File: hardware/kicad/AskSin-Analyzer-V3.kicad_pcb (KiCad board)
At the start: 4 copper layers, 88 x 42 mm, 38 parts, among them J1 Pi GPIO, J2 AVR-ISP-6, J5 OLED I2C, J6 Taster, J7 WS2812, U1 MCP1754S-3302xCB, U2 ATmega328P-AU, U3 E07-900M10S, Y1 8MHz

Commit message: R5 von 0 Ohm auf 330 Ohm — der Serienwiderstand des Vorbilds fehlte
Das Status-LED-OLED-Projekt fuehrt die WS2812-Datenleitung fuer *beide*
Ansteuerarten ueber 330-470 Ohm. Auf dem SPI-Weg war R5 bei uns eine
0-Ohm-Bruecke, der Widerstand fehlte dort also ganz. Jetzt 330 Ohm —
dasselbe Bauteil wie R1 (JLCPCB C17630), damit faellt sogar eine
Position in der Stueckliste weg (10 statt 11).

Signaltechnisch geprueft: 330 Ohm an der Eingangskapazitaet der LED
ergibt rund 5 ns Anstiegszeit gegen 420 ns kuerzeste Pulsdauer bei
2,4 MHz — unkritisch.

DRC 0/0, Netzliste exakt, alle Massepads angebunden.

Co-Authored-By: Claude Opus 5 <noreply@anthropic.com>
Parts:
- R5: value 0R -> 330
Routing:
- net GND: track 31.8 -> 56.5 mm, vias 131 -> 147
- net +3V3: track 134.5 -> 152.2 mm
- net MISO: track 71.8 -> 82.2 mm
- net PI_RESET_DRV: track 46.2 -> 39.8 mm
- net WS_DATA: track 8.16 -> 11.7 mm
- net UART_PI_TX: track 50.3 -> 52.7 mm, vias 2 -> 1
- net RESET: track 56.9 -> 54.9 mm, vias 1 -> 2
- net LED_PWM: track 33.4 -> 35.2 mm
- net SCK: track 66.3 -> 64.7 mm
- net MOSI: track 57.8 -> 56.3 mm, vias 3 -> 2
- net PI_3V3: track 77.9 -> 76.4 mm
- net XTAL1: track 9.97 -> 8.57 mm
- net LED_TREIBER: track 21.6 -> 22.6 mm
- net LED_SPI: track 28.4 -> 29.1 mm
- net CS: track 86.8 -> 87.5 mm

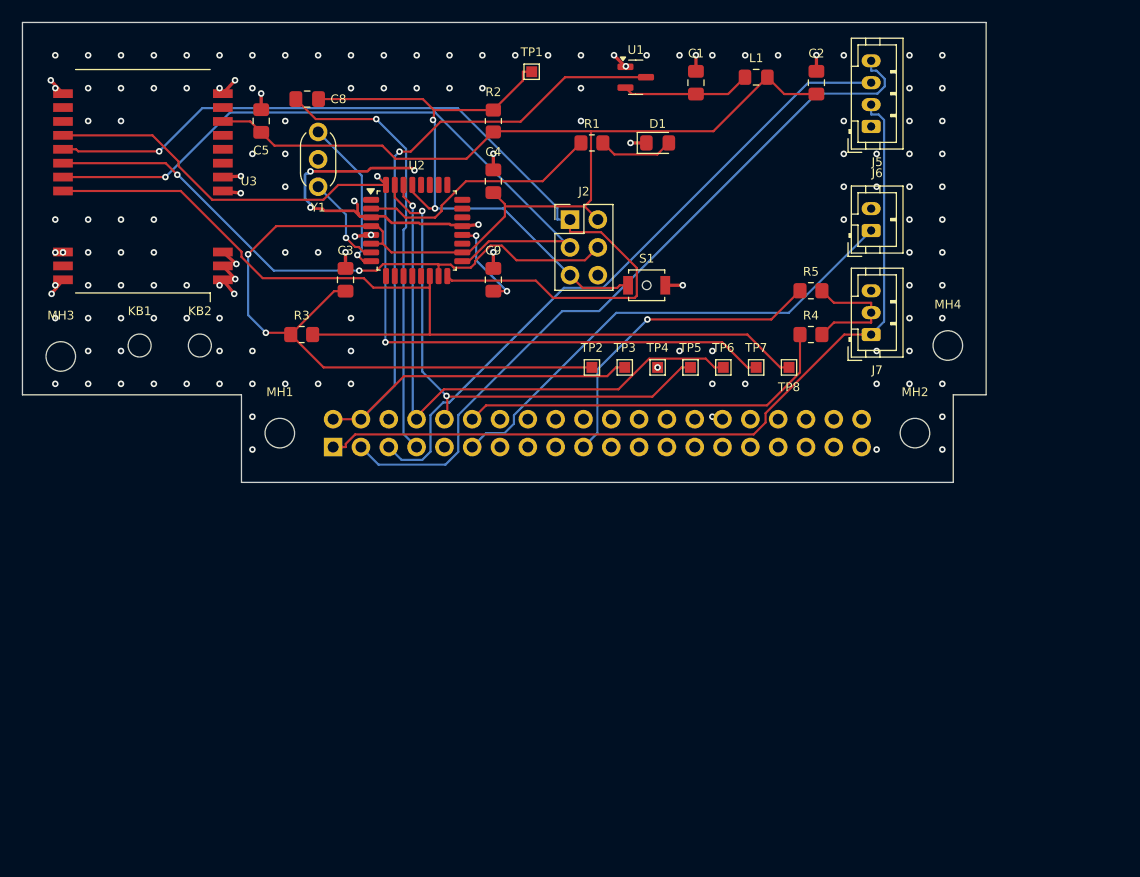
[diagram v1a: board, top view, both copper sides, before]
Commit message: Platine v0.2.0: L-Form neben dem Pi, Umschalter statt Bestueckungsvariante
Neue Bauform nach Silvios Vorgaben: Streifen hoechstens 20 mm neben dem
Pi (vorher 34), bis 80 mm lang, Schenkel an der SD-Kante entlang. Ueber
dem Pi liegt nur der 8 mm tiefe Arm fuer die 2x20-Buchse und eine
7 x 9 mm grosse Nase am hinteren Befestigungsloch — der Luefter des
PoE-HAT bleibt frei, unabhaengig vom Modell. Vier Schraubpunkte: zwei
HAT-Bohrungen im Arm, das hintere Pi-Loch in der Nase, eines im
Schenkel fuer den Tray.

Pi-Masse aus den amtlichen Zeichnungen geprueft: 85 x 56 mm, Loecher
58 x 49 mm, 3,5 mm von den Kanten — bei Pi 3B+, 4 und 5 identisch. Beim
PoE HAT (F) beginnt der Luefter rund 20 mm hinter der SD-Kante.

R4/R5 als Bestueckungsvariante entfallen. Stattdessen SPDT-Schiebe-
schalter SW1 (C&K JS102011SAQN, JLCPCB C221660) an der Aussenkante plus
EIN gemeinsamer 330-Ohm-Widerstand. Bewusst dieser Typ und nicht der
billigere MSK-12C02: fuer den JS102011SAQN gibt es einen amtlichen
KiCad-Footprint, der MSK haette von Hand gezeichnet werden muessen —
seine Landzeichnung hat ungleich verteilte Pads, das ist genau die
Sorte Fehlerquelle, die wir uns nicht leisten koennen.

Zwei eigene Fehler unterwegs gefunden und behoben: Der Innenversatz der
Kontur lief an den einspringenden Ecken in die falsche Richtung, wodurch
Freerouting Bahnen ueber die Platinenkante legte; und der Versuch, In2
als dritte Signallage freizugeben, erzeugte 120 Verstoesse inklusive
echter Kurzschluesse, weil die Stuetzvias durchgehend sind — beides
zurueckgenommen bzw. korrigiert und im Code kommentiert.

ERC 0/0, DRC 0/0, Netzliste exakt gegen die Spezifikation, alle
Massepads angebunden, J1-Pads gegen das Pi-Raster geprueft.
Fertigungspaket neu erzeugt (11 Positionen, davon 7 Basic).

Co-Authored-By: Claude Opus 5 <noreply@anthropic.com>
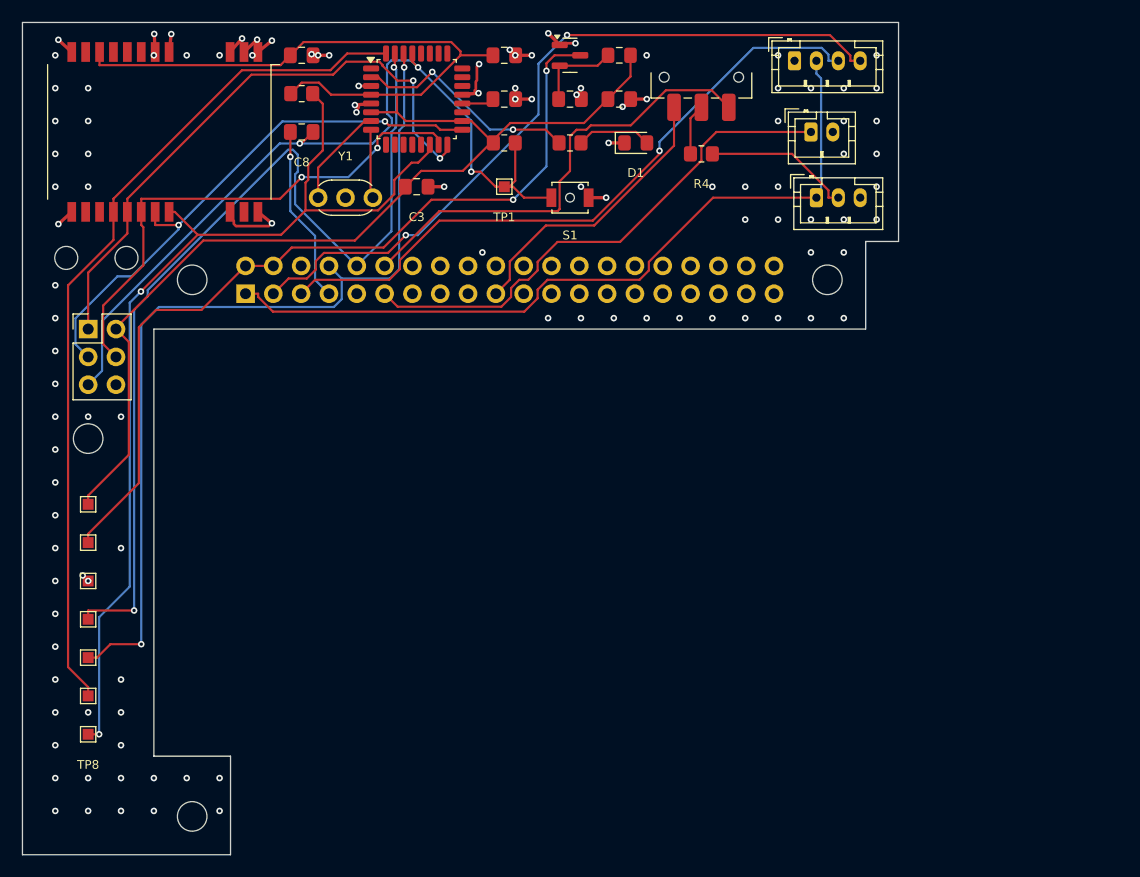
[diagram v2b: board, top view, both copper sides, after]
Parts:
- removed R5: 330, R_0805_2012Metric_Pad1.20x1.40mm_HandSolder
- added SW1: PWM/SPI, SW_SPDT_CK_JS102011SAQN, F.Cu at (162.0, 65.0)
- R4: value 390 DNP -> 330
- moved MH4 79.0 mm to (106.0, 98.0)
- moved TP8 72.2 mm to (106.0, 125.0)
- moved TP7 68.0 mm to (106.0, 121.5)
- moved TP6 63.8 mm to (106.0, 118.0)
- moved TP5 59.6 mm to (106.0, 114.5)
- moved TP4 55.5 mm to (106.0, 111.0)
- moved TP3 51.5 mm to (106.0, 107.5)
- moved TP2 47.7 mm to (106.0, 104.0)
- moved J2 45.1 mm to (106.0, 88.0)
- moved MH3 43.7 mm to (115.5, 132.5)
- moved R3 22.0 mm to (125.5, 66.5)
- moved R4 19.3 mm to (162.0, 72.0)
- moved C2 18.1 mm to (154.5, 67.0), turned to 0 degrees
- moved C9 16.5 mm to (144.0, 67.0), turned to 0 degrees
- moved J1 16.1 mm to (120.4, 84.8)
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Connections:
- R4 pad 1: LED_PWM -> WS_WAHL
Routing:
- net UART_328_TX: track 47.7 -> 87.6 mm
- net UART_PI_TX: track 52.7 -> 82.8 mm, vias 1 -> 2
- net MISO: track 82.2 -> 55.1 mm, vias 1 -> 2
- net PI_RESET_DRV: track 39.8 -> 16.2 mm
- net RESET: track 54.9 -> 76.3 mm, vias 2 -> 3
- net GND: track 56.5 -> 37.8 mm, vias 147 -> 114
- net SCK: track 64.7 -> 50.7 mm, vias 1 -> 2
- net MOSI: track 56.3 -> 47.4 mm
- net XTAL2: track 14.6 -> 6.31 mm, vias 1 -> 0
- net LED_PWM: track 35.2 -> 42.1 mm
- net GDO0: track 84.1 -> 78.3 mm, vias 2 -> 0
- net AREF: track 8.77 -> 2.97 mm, vias 2 -> 0
- net PI_3V3: track 76.4 -> 71.1 mm
- net +3V3: track 152.2 -> 147.4 mm, vias 2 -> 0
- net WS_WAHL: track 0.00 -> 4.66 mm
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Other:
- board size 88 x 42 mm -> 80 x 76 mm

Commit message: Platine 100 mm lang, Schalter beschriftet, Fertigungspruefung als Skript
Laenge von 80 auf 100 mm — die zusaetzliche Flaeche entspannt Routing und
Bestueckungsdruck deutlich; der Streifen neben dem Pi bleibt bei 20 mm.
Fuenfter Schraubpunkt am vorderen Ende fuer den Tray.

Der Umschalter traegt jetzt „PWM" und „SPI" im Bestueckungsdruck. Die
Beschriftung benennt bewusst die **Anschluesse** (Pin 1 = GPIO18,
Pin 3 = GPIO10), nicht die Schieberstellungen: welche Stellung welchen
Anschluss durchschaltet, gibt C&K nicht frei zugaenglich her, die
Pinbelegung dagegen steht fest. Positionen leiten sich aus den echten
Pads ab, folgen also einer Umplatzierung automatisch.

Neu: pruefe_fertigung.py — 17 maschinelle Pruefungen ueber das hinaus,
was DRC und Netzlistenvergleich abdecken: Lagenaufbau, geschlossener
Umriss, kleinster Bohrer und Via-Ring gegen die Herstellermindestmasse,
Bohrbild gegen das Pi-Raster, J1 gegen die HAT-Vorlage, Polung der
Status-LED, Verdrahtung und Beschriftung des Schalters, Vollstaendigkeit
des Archivs, Deckungsgleichheit von BOM/CPL/Platine.

Das Skript hat prompt zwei Abweichungen gemeldet — beide in ihm selbst:
Der Ursprung kam aus der Bounding-Box, die die halbe Linienbreite der
Umrisskante mitzaehlt (0,05 mm Versatz gegen die Fertigungsdaten). Jetzt
rechnet es aus den Kantensegmenten. Ausserdem meidet die Beschriftungs-
routine nun jedes einzelne Pad, nicht nur Bauteilumrisse.

Ergebnis: DRC 0/0, ERC 0/0, Netzliste exakt, alle 17 Pruefungen bestanden.

Co-Authored-By: Claude Opus 5 <noreply@anthropic.com>
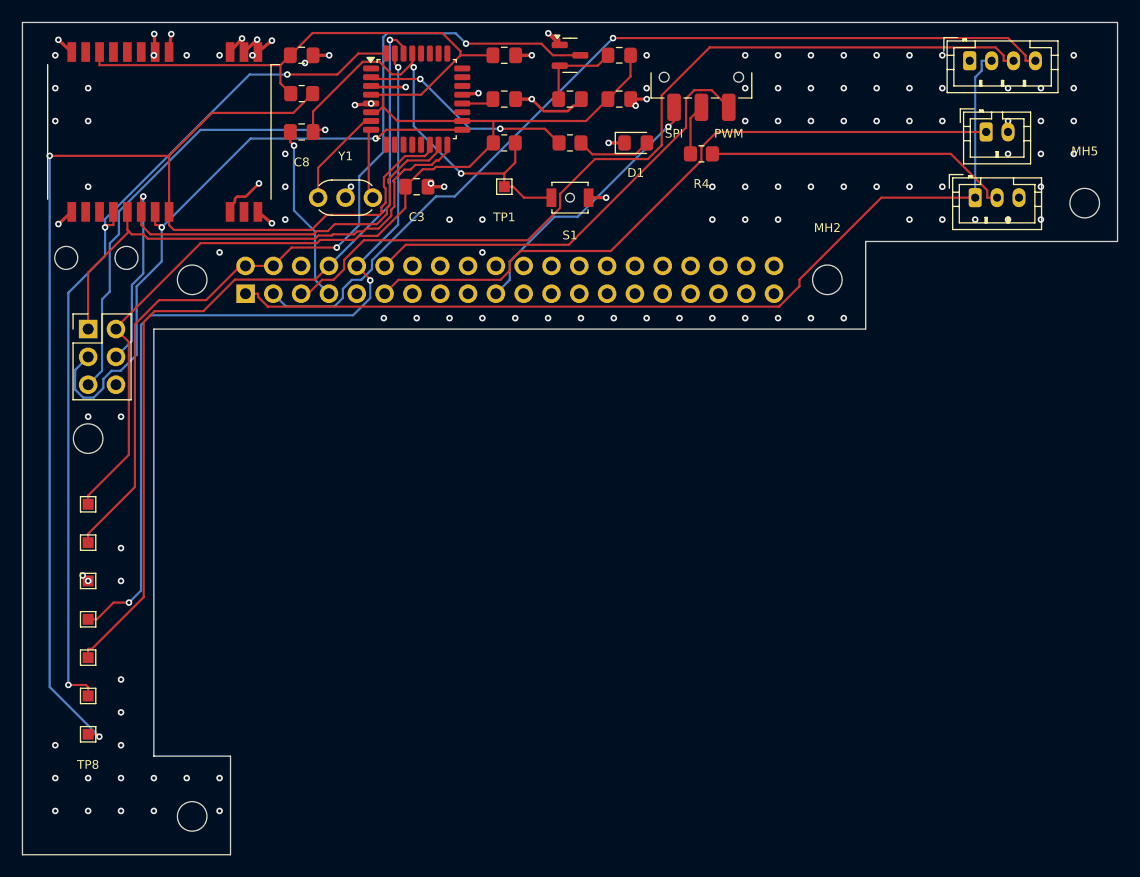
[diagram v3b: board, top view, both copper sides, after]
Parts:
- added MH5: MountingHole_2.7mm_M2.5, MountingHole_2.7mm_M2.5, F.Cu at (197.0, 76.5)
- moved J5 16.0 mm to (186.5, 63.5)
- moved J6 16.0 mm to (188.0, 70.0)
- moved J7 14.5 mm to (187.0, 76.0)
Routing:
- net CS: track 91.2 -> 118.2 mm
- net I2C_SCL: track 60.3 -> 79.1 mm, vias 1 -> 0
- net BTN: track 47.7 -> 62.2 mm
- net I2C_SDA: track 67.8 -> 82.3 mm, vias 2 -> 1
- net WS_DATA: track 13.6 -> 28.1 mm
- net PI_3V3: track 71.1 -> 85.4 mm
- net UART_328_TX: track 87.6 -> 76.7 mm, vias 2 -> 3
- net MISO: track 55.1 -> 47.4 mm, vias 2 -> 0
- net SCK: track 50.7 -> 57.1 mm
- net UART_PI_TX: track 82.8 -> 77.0 mm, vias 2 -> 1
- net +5V: track 77.7 -> 83.0 mm
- net MOSI: track 47.4 -> 51.5 mm, vias 2 -> 1
- net GND: track 37.8 -> 41.8 mm, vias 114 -> 128
- net +3V3: track 147.4 -> 143.9 mm
- net RESET: track 76.3 -> 79.6 mm
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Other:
- board size 80 x 76 mm -> 100 x 76 mm
- board text added: "PWM"
- board text added: "SPI"

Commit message: Platine: Verlaengerung nach HINTEN statt nach vorn — Korrektur
Silvio hat es rechtzeitig bemerkt: Beim Vergroessern auf 100 mm hatte ich
die zusaetzlichen 20 mm nach vorn gelegt, wodurch die Platine 3 mm ueber
die Buchsenseite des Pi hinausragte — genau dorthin, wo im 19-Zoll-Einbau
die Keystone-Module sitzen. Die Verlaengerung gehoert hinter die SD-Kante.

Der Schenkel ist jetzt 32 statt 12 mm tief; die Platine endet 17 mm vor
dem vorderen Pi-Ende, also genauso weit wie beim 80-mm-Entwurf. Die
gewonnene Flaeche hinter dem Pi nimmt das Funkmodul auf (17,5 x 21 mm,
im 20-mm-Streifen ging es nur quer), dazu ISP und Pruefpunkte. Das
entlastet den Streifen deutlich — das Routing geht seither durch.

Damit dieser Fehler nicht wiederkehren kann, prueft pruefe_fertigung.py
jetzt die Einbaumasse hart: Streifenbreite <= 20 mm, Gesamtlaenge
<= 100 mm, **kein Ueberstand ueber die Buchsenseite**, ueber dem Pi
hoechstens 10 mm Material. Ausserdem meidet die Platzsuche fuer die
Platinenmarkierung jetzt jedes Pad und jedes Via — die feinere
Unterscheidung nach Seite und Abdeckung hatte Loecher.

DRC 0/0, ERC 0/0, Netzliste exakt, alle 21 Fertigungspruefungen bestanden.

Co-Authored-By: Claude Opus 5 <noreply@anthropic.com>
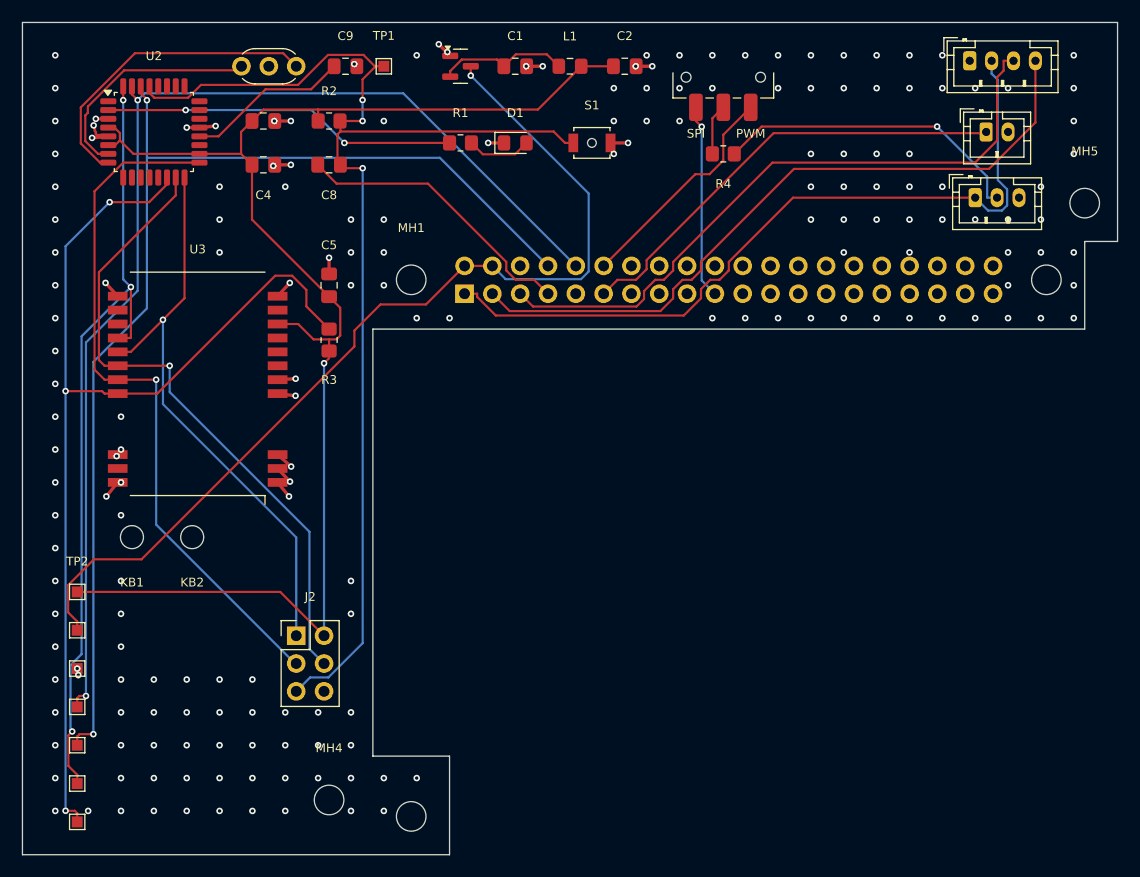
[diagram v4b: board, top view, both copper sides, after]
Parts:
- moved MH4 39.7 mm to (128.0, 131.0)
- moved J2 33.8 mm to (125.0, 116.0)
- moved KB1 26.2 mm to (110.0, 107.0)
- moved KB2 26.2 mm to (115.5, 107.0)
- moved U2 24.2 mm to (112.0, 70.0)
- moved C4 24.2 mm to (122.0, 73.0)
- moved U3 23.3 mm to (116.0, 93.0), turned to 0 degrees
- moved R3 22.6 mm to (128.0, 89.0), turned to 90 degrees
- moved C5 21.1 mm to (128.0, 84.0), turned to 90 degrees
- moved J1 20.0 mm to (140.4, 84.8)
- moved MH1 20.0 mm to (135.5, 83.5)
- moved MH2 20.0 mm to (193.5, 83.5)
- moved MH3 20.0 mm to (135.5, 132.5)
- moved R2 16.1 mm to (128.0, 69.0)
- moved TP1 15.6 mm to (133.0, 64.0)
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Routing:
- net RESET: track 79.6 -> 111.1 mm
- net UART_328_TX: track 76.7 -> 106.3 mm, vias 3 -> 2
- net UART_PI_TX: track 77.0 -> 104.5 mm, vias 1 -> 2
- net XTAL2: track 6.44 -> 28.7 mm
- net CS: track 118.2 -> 97.2 mm, vias 2 -> 3
- net BTN: track 62.2 -> 41.5 mm
- net LED_PWM: track 40.3 -> 20.8 mm
- net I2C_SCL: track 79.1 -> 59.6 mm
- net I2C_SDA: track 82.3 -> 64.0 mm, vias 1 -> 0
- net PI_3V3: track 85.4 -> 70.4 mm
- net LED_TREIBER: track 19.6 -> 32.4 mm
- net XTAL1: track 9.34 -> 21.4 mm
- net AREF: track 2.97 -> 15.0 mm
- net +3V3: track 143.9 -> 132.5 mm, vias 0 -> 1
- net GND: track 41.8 -> 30.4 mm, vias 128 -> 184
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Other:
- outline, holes or cut-outs redrawn

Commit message: Peripheriestecker beschriftet, Token-Feld mit Umschalter anzeigen/verbergen
Platine
-------
J5, J6 und J7 sind baugleiche JST-PH-Buchsen und unterscheiden sich nur in der
Polzahl — am fertigen Geraet war nicht zu erkennen, welche das OLED, welche den
Taster und welche die WS2812 aufnimmt. Sie tragen jetzt ihre Funktion im
Bestueckungsdruck: OLED I2C, TASTER, WS2812.

Der Text kommt aus dem Schaltplanwert, nicht aus einer zweiten Liste, und der
Platz wird gesucht statt festgelegt: vier Kandidaten rund um die Buchse, der
erste freie gewinnt. Findet sich keiner, bricht der Lauf ab, statt still eine
unbeschriftete Buchse auszuliefern.

pruefe_fertigung.py prueft das jetzt hart: Zu jeder Buchse muss ein Aufdruck
mit dem Schaltplanwert existieren und hoechstens 15 mm entfernt stehen.
Gegentest gefahren — ohne den Aufdruck meldet die Pruefung den Fehler.

Nebenbei zwei Altlasten beseitigt: Die lesbare Stueckliste meldete "+ R4 als
DNP dokumentiert" und die DNP-Zeile nannte eine "PWM-Alternative zu R5". R5
gibt es seit dem Schiebeschalter nicht mehr, unbestueckt ist nichts.

Platinenmarkierung
------------------
Die zweizeilige Markierung braucht einen zusammenhaengenden freien Block von
rund 30 x 6 mm, der Schenkel hinter dem Pi ist aber nur 32 mm breit. Ob das
gelang, entschied die Zufallslage der Vias — acht Neubauten scheiterten
hintereinander mit "Kein freier Platz", obwohl am Layout nichts falsch war.
Jetzt werden vier Fassungen der Reihe nach probiert, von gross und zweizeilig
bis klein und vierzeilig.

Weboberflaeche
--------------
Neue Komponente GeheimFeld: Eingabefeld fuer ein Geheimnis mit Umschalter
"anzeigen / verbergen". Ein verdecktes Feld verhindert Mitlesen, macht aber
jeden Tippfehler unsichtbar — und ein falscher Token aeussert sich nur als
"nicht berechtigt". Eingesetzt am Auth-Token, am Peer-Token und am
InfluxDB-Token.

Pruefstand: DRC 0 Verstoesse / 0 unverbundene Pads, alle 30 maschinellen
Pruefungen bestanden, Gerber Zeichen fuer Zeichen aus der ak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
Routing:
- net GND: track 30.4 -> 114.5 mm, vias 184 -> 208
- net UART_PI_TX: track 104.5 -> 115.8 mm
- net UART_328_TX: track 106.3 -> 115.4 mm, vias 2 -> 3
- net +5V: track 88.9 -> 97.0 mm
- net XTAL2: track 28.7 -> 20.8 mm, vias 0 -> 1
- net XTAL1: track 21.4 -> 27.3 mm
- net CS: track 97.2 -> 91.4 mm, vias 3 -> 2
- net SCK: track 64.2 -> 60.1 mm
- net MOSI: track 59.3 -> 62.1 mm
- net +3V3: track 132.5 -> 135.1 mm, vias 1 -> 0
- net RESET: track 111.1 -> 108.7 mm, vias 3 -> 2
- net GDO0: track 72.6 -> 70.3 mm
- net LED_TREIBER: track 32.4 -> 33.8 mm
- net MISO: track 53.0 -> 53.8 mm
- net PI_3V3: track 70.4 -> 71.1 mm
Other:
- board text added: "OLED I2C"
- board text added: "TASTER"
- board text added: "WS2812"
